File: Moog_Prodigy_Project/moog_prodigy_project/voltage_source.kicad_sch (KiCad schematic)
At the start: 20 parts, among them J6 Conn_01x02_Socket, SW8 SW_DPST, T1 230 VAC/ 15VAC 1.5A 22W, U75 L78L12, U76 L79L12

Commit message: PCB priprema i fix gresaka
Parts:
- J6: footprint Connector_PinSocket_2.54mm:PinSocket_1x01_P2.54mm_Horizontal -> Connector_PinSocket_2.54mm:PinSocket_1x02_P2.54mm_Vertical
- SW8: footprint Connector_PinSocket_2.54mm:PinSocket_1x01_P2.54mm_Horizontal -> 471016264143_dupli_prekidac:471016264143_2_00-3_00_
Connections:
- net GND: now also T1.4 (SA); no longer T1.3 (SA)
- net kraj_2: now also T1.3 (AB); no longer T1.2 (AB)
- net at F2.1: now also T1.6 (SB); no longer T1.4 (SB)
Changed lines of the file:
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@@
 		(pin "1"
 		)
-		(pin "2"
+		(pin "6"
 		)
 		(pin "3"
@@
 			)
 		)
-		(property "Footprint" "Connector_PinSocket_2.54mm:PinSocket_1x01_P2.54mm_Horizontal"
+		(property "Footprint" "471016264143_dupli_prekidac:471016264143_2_00-3_00_"
 			(at 54.61 49.53 0)
 			(effects
@@
 			)
 		)
-		(property "Footprint" "Connector_PinSocket_2.54mm:PinSocket_1x01_P2.54mm_Horizontal"
+		(property "Footprint" "Connector_PinSocket_2.54mm:PinSocket_1x02_P2.54mm_Vertical"
 			(at 33.02 52.07 0)
 			(effects

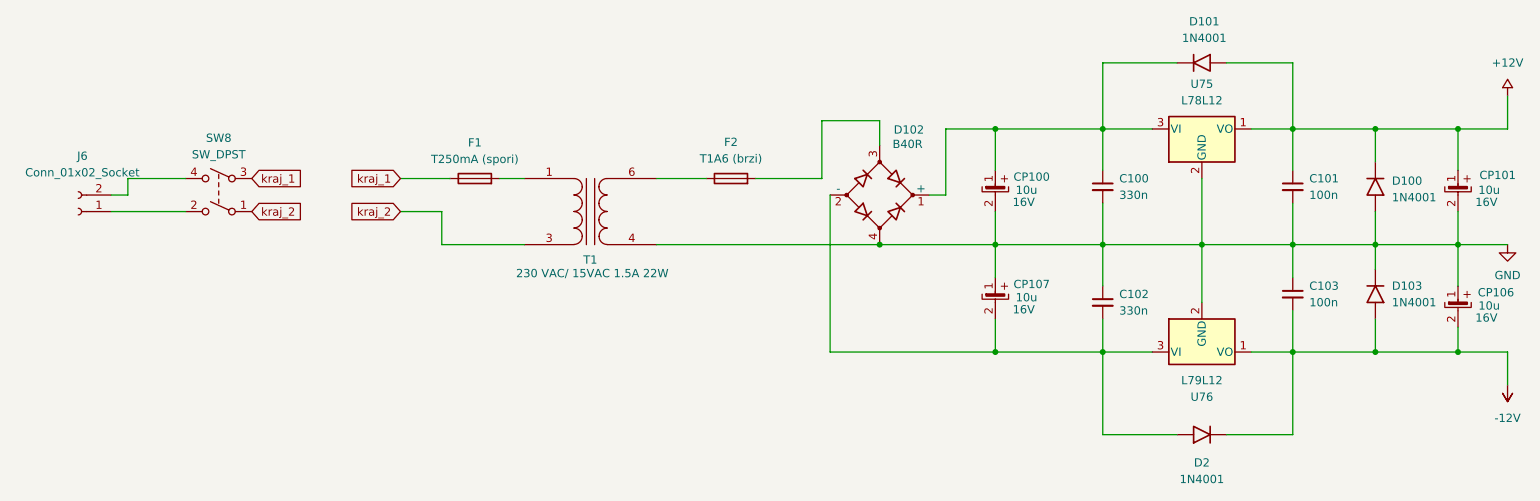
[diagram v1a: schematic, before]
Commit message: problemi sa ca3096, multiplicirani footprintovi
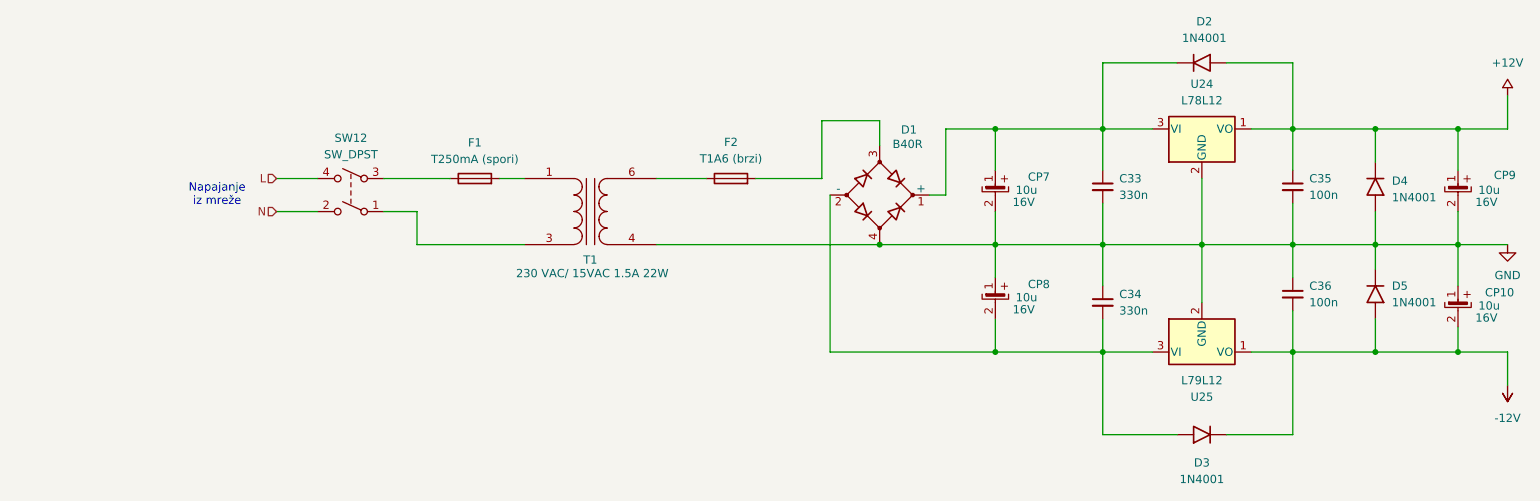
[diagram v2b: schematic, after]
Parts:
- removed J6: Conn_01x02_Socket, Connector_PinSocket_2.54mm:PinSocket_1x02_P2.54mm_Vertical, symbol Connector:Conn_01x02_Socket
- renumbered C100 to C33, C102 to C34, C101 to C35, C103 to C36, CP106 to CP10, CP100 to CP7, CP107 to CP8, CP101 to CP9, D102 to D1, D101 to D2, D2 to D3, D100 to D4, D103 to D5, SW8 to SW12, U75 to U24, U76 to U25
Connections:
- net N: now reaches SW12.2
- net L: now reaches SW12.4
- net kraj_1: no longer names the net of F1.1, SW12.3
- net kraj_2: no longer names the net of SW12.1, T1.3 (AB)
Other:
- note added: "Napajanje iz mreže"
- moved on the sheet: SW12

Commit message: Routhed PCB final 17.05.2026
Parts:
- removed SW12: SW_DPST, 471016264143_dupli_prekidac:471016264143_2_00-3_00_, symbol Switch:SW_DPST
- added Double_Switch1: 200MDP1T1B1M2QEH, 200MDP1T1B1M2QEH:SW_200MDP1T1B1M2QEH, symbol 200MDP1T1B1M2QEH:200MDP1T1B1M2QEH
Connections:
- net L: now also Double_Switch1.2
- net N: now also Double_Switch1.5
- net at T1.3 (AB): now also Double_Switch1.6
- net at F1.1: now also Double_Switch1.1
- no-connect marks 0 -> 2
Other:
- moved on the sheet: F1

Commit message: Latest checkpoints update 05.06.2026
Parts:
- renumbered Double_Switch1 to Dupli_preklopnik
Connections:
- net +12V: now also CP9.; no longer CP9.1
- net -12V: now also CP10.; no longer CP10.2
- net GND: now also CP10., CP7., CP8., CP9.; no longer CP10.1, CP7.2, CP8.1, CP9.2
- net at C33.1, D1.1 (+), D2.1 (K)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: now also CP7.; no longer CP7.1
- net at C34.2, D1.2 (-), D3.2 (A)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: now also CP8.; no longer CP8.2
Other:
- moved on the sheet: D3
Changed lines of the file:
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@@
 	(wire
 		(pts
-			(xy 190.5 86.36) (xy 190.5 73.66)
+			(xy 190.5 83.82) (xy 190.5 73.66)
 		)
 		(stroke
@@
 	(wire
 		(pts
-			(xy 219.71 86.36) (xy 219.71 73.66)
+			(xy 219.71 83.82) (xy 219.71 73.66)
 		)
 		(stroke
@@
 	(wire
 		(pts
-			(xy 209.55 86.36) (xy 219.71 86.36)
+			(xy 209.55 83.82) (xy 219.71 83.82)
 		)
 		(stroke
@@
 	(wire
 		(pts
-			(xy 201.93 86.36) (xy 190.5 86.36)
+			(xy 201.93 83.82) (xy 190.5 83.82)
 		)
 		(stroke
@@
 		(on_board yes)
 		(dnp no)
-		(fields_autoplaced yes)
-		(property "Reference" "Double_Switch1"
-			(at 68.58 39.37 0)
+		(property "Reference" "Dupli_preklopnik"
+			(at 69.596 41.656 0)
 			(effects
 				(font
@@
 					(size 1.27 1.27)
 				)
+				(hide yes)
 			)
 		)
@@
 			(project "moog_prodigy_project"
 				(path "/db469bdb-b6c3-4a16-9199-d4e6b8d556e8/632a0a15-d2db-46b0-8553-670bc8b18225"
-					(reference "Double_Switch1")
+					(reference "Dupli_preklopnik")
 					(unit 1)
 				)
@@
 		(dnp no)
 		(property "Reference" "CP10"
-			(at 253.746 64.516 0)
+			(at 245.11 63.5 0)
 			(effects
 				(font
@@
 			)
 		)
-		(pin "1"
-		)
-		(pin "2"
+		(pin ""
+		)
+		(pin ""
 		)
 		(instances
@@
 		(lib_name "1N4001_1")
 		(lib_id "Diode:1N4001")
-		(at 205.74 86.36 180)
+		(at 205.74 83.82 180)
 		(unit 1)
 		(exclude_from_sim no)
@@
 		(dnp no)
 		(property "Reference" "D3"
-			(at 205.74 90.678 0)
+			(at 205.74 86.614 0)
 			(effects
 				(font
@@
 		)
 		(property "Value" "1N4001"
-			(at 205.74 93.218 0)
+			(at 205.74 88.392 0)
 			(effects
 				(font
@@
 		)
 		(property "Footprint" "Diode_THT:D_DO-41_SOD81_P10.16mm_Horizontal"
-			(at 205.74 84.074 0)
+			(at 205.74 81.534 0)
 			(effects
 				(font
@@
 		)
 		(property "Datasheet" "http://www.vishay.com/docs/88503/1n4001.pdf"
-			(at 205.74 83.312 0)
+			(at 205.74 80.772 0)
 			(effects
 				(font
@@
 		)
 		(property "Description" ""
-			(at 205.74 86.36 0)
+			(at 205.74 83.82 0)
 			(effects
 				(font
@@
 		)
 		(property "Sim.Device" "D"
-			(at 205.613 83.312 0)
+			(at 205.613 80.772 0)
 			(effects
 				(font
@@
 		)
 		(property "Sim.Pins" "1=K 2=A"
-			(at 205.613 83.312 0)
+			(at 205.613 80.772 0)
 			(effects
 				(font
@@
 		(dnp no)
 		(property "Reference" "CP7"
-			(at 182.372 46.736 0)
+			(at 172.974 45.466 0)
 			(effects
 				(font
@@
 		)
 		(property "Value" "10u"
-			(at 180.4416 48.768 0)
+			(at 180.34 47.752 0)
 			(effects
 				(font
@@
 		)
 		(property "Rated Voltage" "16V"
-			(at 178.3588 50.6222 0)
-			(effects
-				(font
-					(size 1.27 1.27)
-				)
-			)
-		)
-		(pin "1"
-		)
-		(pin "2"
+			(at 178.562 50.038 0)
+			(effects
+				(font
+					(size 1.27 1.27)
+				)
+			)
+		)
+		(pin ""
+		)
+		(pin ""
 		)
 		(instances
@@
 		(on_board yes)
 		(dnp no)
-		(fields_autoplaced yes)
 		(property "Reference" "D4"
-			(at 234.95 47.3586 90)
+			(at 234.696 48.768 90)
 			(effects
 				(font
@@
 		)
 		(property "Value" "1N4001"
-			(at 234.95 49.8986 90)
+			(at 232.664 51.054 90)
 			(effects
 				(font
@@
 		(dnp no)
 		(property "Reference" "F1"
-			(at 95.25 41.4782 90)
+			(at 95.25 42.418 90)
 			(effects
 				(font
@@
 		)
 		(property "Value" "T250mA (spori)"
-			(at 96.774 44.196 90)
+			(at 97.282 44.45 90)
 			(effects
 				(font
@@
 		(on_board yes)
 		(dnp no)
-		(fields_autoplaced yes)
 		(property "Reference" "D2"
-			(at 206.1087 22.86 0)
+			(at 205.74 24.892 0)
 			(effects
 				(font
@@
 		)
 		(property "Value" "1N4001"
-			(at 206.1087 25.4 0)
+			(at 205.74 26.924 0)
 			(effects
 				(font
@@
 		(on_board yes)
 		(dnp no)
-		(fields_autoplaced yes)
 		(property "Reference" "D5"
-			(at 234.95 63.4999 90)
+			(at 234.95 65.278 90)
 			(effects
 				(font
@@
 		)
 		(property "Value" "1N4001"
-			(at 234.95 66.0399 90)
+			(at 232.664 67.564 90)
 			(effects
 				(font
@@
 	)
 	(symbol
-		(lib_name "elektrolit_3")
+		(lib_name "elektrolit_4")
 		(lib_id "elektrolitski:elektrolit")
 		(at 173.99 64.77 0)
@@
 		(dnp no)
 		(property "Reference" "CP8"
-			(at 182.372 63.246 0)
+			(at 172.974 62.992 0)
 			(effects
 				(font
@@
 		)
 		(property "Value" "10u"
-			(at 180.4416 65.278 0)
+			(at 180.1368 64.1858 0)
 			(effects
 				(font
@@
 		)
 		(property "Rated Voltage" "16V"
-			(at 178.3588 67.1322 0)
-			(effects
-				(font
-					(size 1.27 1.27)
-				)
-			)
-		)
-		(pin "1"
-		)
-		(pin "2"
+			(at 178.054 66.04 0)
+			(effects
+				(font
+					(size 1.27 1.27)
+				)
+			)
+		)
+		(pin ""
+		)
+		(pin ""
 		)
 		(instances
@@
 		(dnp no)
 		(property "Reference" "CP9"
-			(at 254 46.482 0)
+			(at 244.602 46.482 0)
 			(effects
 				(font
@@
 			)
 		)
-		(pin "1"
-		)
-		(pin "2"
+		(pin ""
+		)
+		(pin ""
 		)
 		(instances

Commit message: 27.06.2026 - dodavanje izmena sa konsultacija
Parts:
- renumbered Dupli_preklopnik to Dupli_preklopnik1
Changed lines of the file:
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@@
 		(comment 1 "Fakultet tehničkih nauka")
 		(comment 2 "Univerzitet u Novom Sadu")
-		(comment 3 "Merno-Informacioni sistemi")
+		(comment 3 "Merno-Informacioni sistemi ")
 	)
 	(text "Napajanje\niz mreže"
@@
 		(on_board yes)
 		(dnp no)
-		(property "Reference" "Dupli_preklopnik"
+		(property "Reference" "Dupli_preklopnik1"
 			(at 69.596 41.656 0)
 			(effects
@@
 			(project "moog_prodigy_project"
 				(path "/db469bdb-b6c3-4a16-9199-d4e6b8d556e8/632a0a15-d2db-46b0-8553-670bc8b18225"
-					(reference "Dupli_preklopnik")
+					(reference "Dupli_preklopnik1")
 					(unit 1)
 				)
